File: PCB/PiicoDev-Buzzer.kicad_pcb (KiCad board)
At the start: 2 copper layers, 25.4 x 25.4 mm, 23 parts, among them J1 , J2 , SW1 ADDR, U1 ATtiny806

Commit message: Change R1 to 10k
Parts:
- R1: value 4k7 -> 10k
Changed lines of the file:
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@@
   (general
     (thickness 1.6)
-    (drawings 51)
+    (drawings 49)
     (tracks 180)
     (zones 0)
@@
     (32 B.Adhes user hide)
     (33 F.Adhes user hide)
-    (34 B.Paste user)
-    (35 F.Paste user)
-    (36 B.SilkS user)
-    (37 F.SilkS user)
-    (38 B.Mask user)
+    (34 B.Paste user hide)
+    (35 F.Paste user hide)
+    (36 B.SilkS user hide)
+    (37 F.SilkS user hide)
+    (38 B.Mask user hide)
     (39 F.Mask user)
     (40 Dwgs.User user)
@@
       (effects (font (size 1 1) (thickness 0.15)))
     )
-    (fp_text value 4k7 (at 0 1.17 90) (layer F.Fab) hide
+    (fp_text value 10k (at 0 1.17 90) (layer F.Fab) hide
       (effects (font (size 1 1) (thickness 0.15)))
     )
@@
   (gr_text 3 (at 99.482 110.546) (layer B.SilkS)
     (effects (font (size 1 1) (thickness 0.2)) (justify mirror))
-  )
-  (dimension 3.5 (width 0.15) (layer Dwgs.User)
-    (gr_text "3.500 mm" (at 108.232 117.976) (layer Dwgs.User)
-      (effects (font (size 1 1) (thickness 0.15)))
-    )
-    (feature1 (pts (xy 106.482 114.776) (xy 106.482 117.262421)))
-    (feature2 (pts (xy 109.982 114.776) (xy 109.982 117.262421)))
-    (crossbar (pts (xy 109.982 116.676) (xy 106.482 116.676)))
-    (arrow1a (pts (xy 106.482 116.676) (xy 107.608504 116.089579)))
-    (arrow1b (pts (xy 106.482 116.676) (xy 107.608504 117.262421)))
-    (arrow2a (pts (xy 109.982 116.676) (xy 108.855496 116.089579)))
-    (arrow2b (pts (xy 109.982 116.676) (xy 108.855496 117.262421)))
   )
   (gr_text "Buzzer\npiico.dev/p18" (at 97.282 94.996) (layer B.SilkS)
@@
   (gr_arc (start 108.712 112.776) (end 108.712 114.046) (angle -90) (layer Edge.Cuts) (width 0.05))
   (gr_arc (start 85.852 112.776) (end 84.582 112.776) (angle -90) (layer Edge.Cuts) (width 0.05))
-  (dimension 1.27 (width 0.15) (layer Dwgs.User)
-    (gr_text "1.270 mm" (at 115.6 108.646 90) (layer Dwgs.User)
-      (effects (font (size 1 1) (thickness 0.15)))
-    )
-    (feature1 (pts (xy 112.014 114.046) (xy 114.886421 114.046)))
-    (feature2 (pts (xy 112.014 112.776) (xy 114.886421 112.776)))
-    (crossbar (pts (xy 114.3 112.776) (xy 114.3 114.046)))
-    (arrow1a (pts (xy 114.3 114.046) (xy 113.713579 112.919496)))
-    (arrow1b (pts (xy 114.3 114.046) (xy 114.886421 112.919496)))
-    (arrow2a (pts (xy 114.3 112.776) (xy 113.713579 113.902504)))
-    (arrow2b (pts (xy 114.3 112.776) (xy 114.886421 113.902504)))
-  )
   (gr_line (start 108.712 114.046) (end 85.852 114.046) (layer Edge.Cuts) (width 0.05))
   (gr_line (start 109.982 91.646) (end 109.982 112.776) (layer Edge.Cuts) (width 0.05))

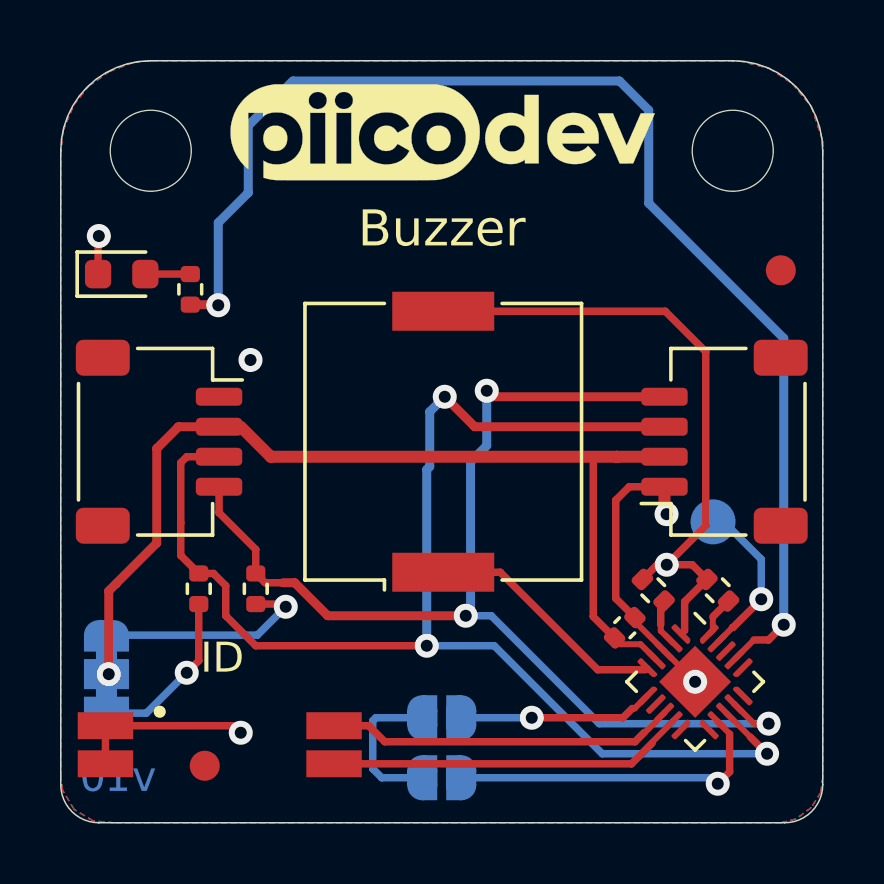
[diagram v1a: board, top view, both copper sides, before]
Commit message: KiCad v5 -> v6
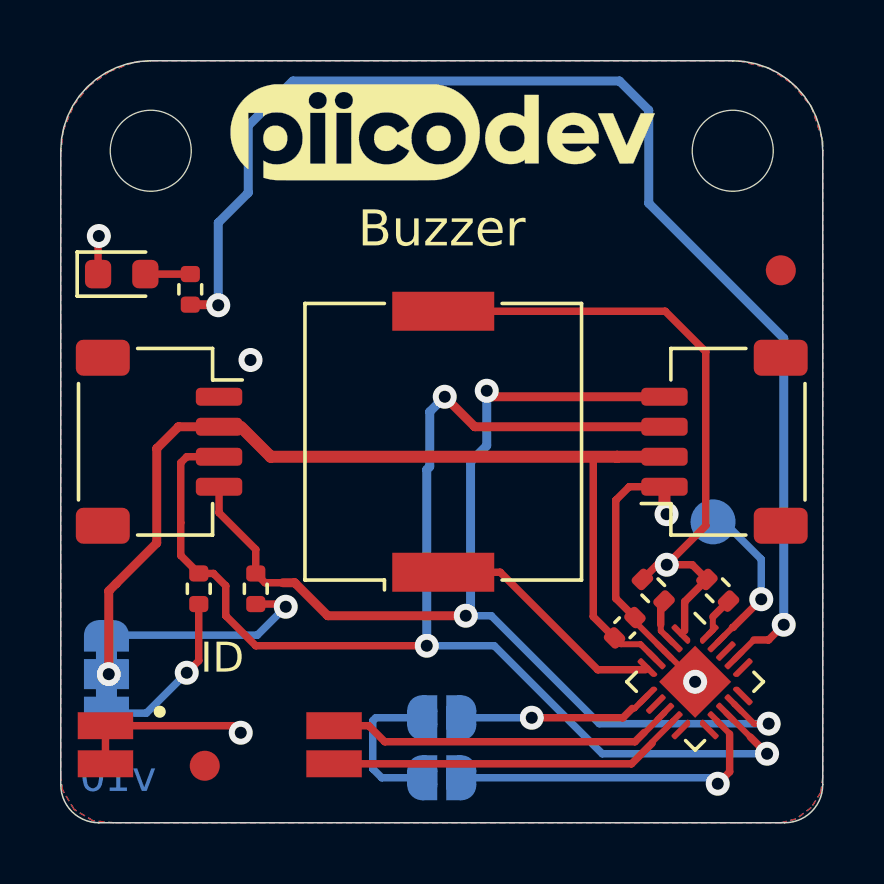
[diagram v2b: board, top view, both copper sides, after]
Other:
- net class Default removed
- net class IC tail removed
- net class Power removed
